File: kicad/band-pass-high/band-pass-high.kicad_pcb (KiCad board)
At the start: 2 copper layers, 154.9 x 25.4 mm, 66 parts, among them J1 Conn_01x06, U1 LF353DR, U2 LF353DR, U3 LF353DR, U4 LM339DR, U5 LM339DR

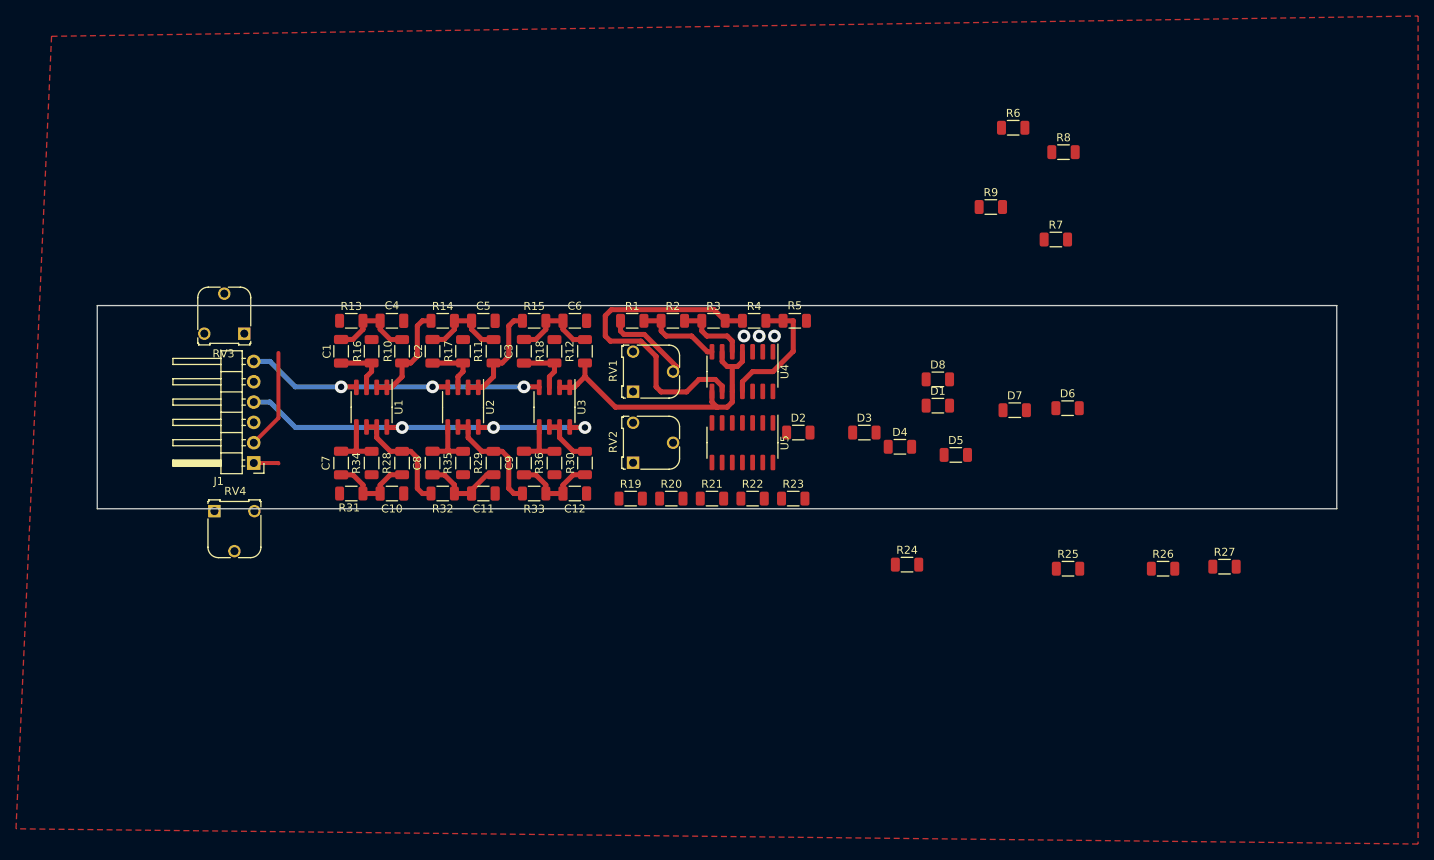
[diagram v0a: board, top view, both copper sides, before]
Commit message: Made a filter PCB design
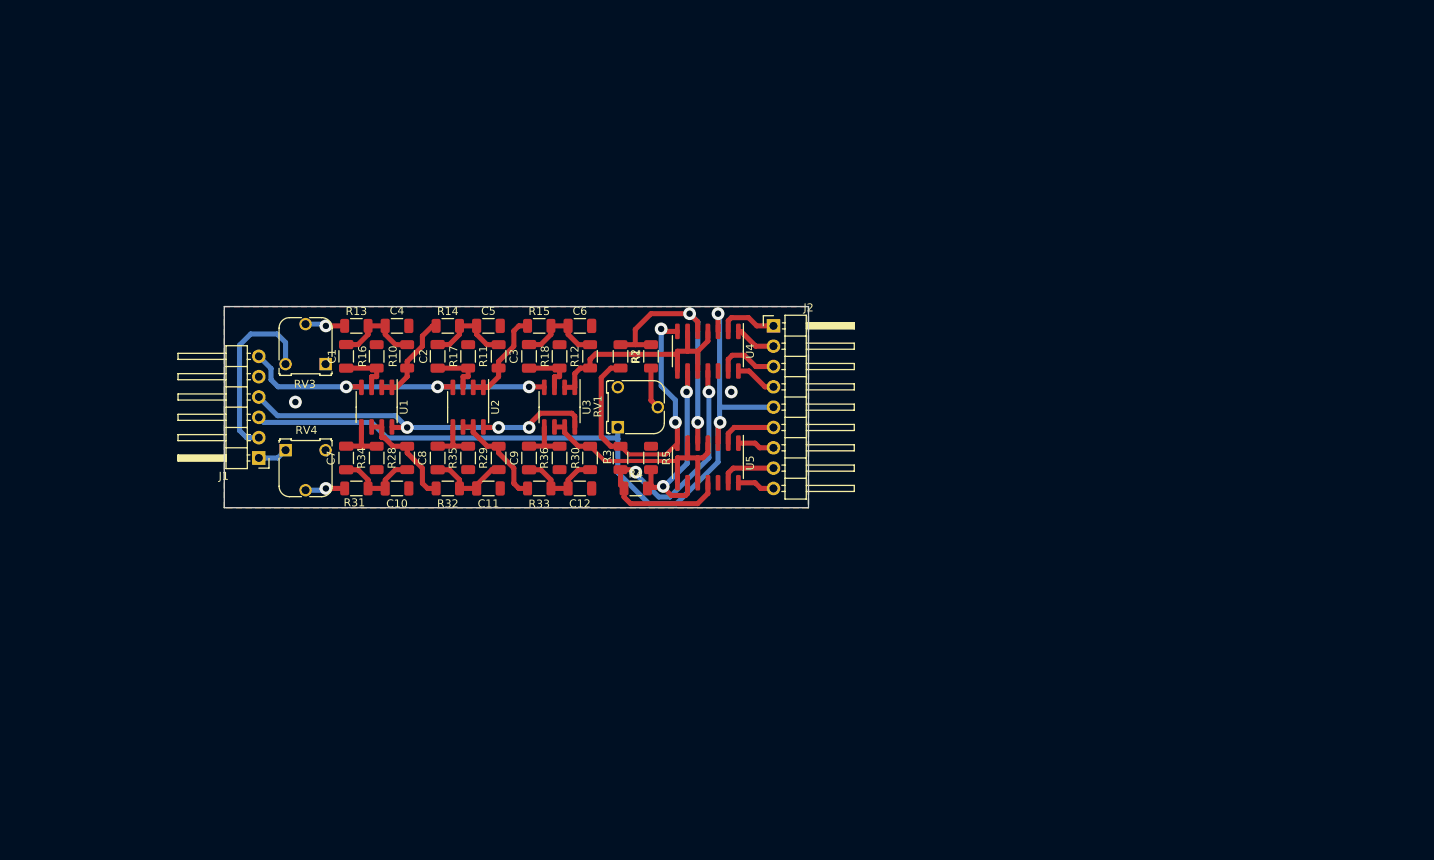
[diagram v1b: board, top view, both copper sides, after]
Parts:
- removed D1, D5: blue, Resistor_SMD:R_1206_3216Metric
- removed D2, D6: green, Resistor_SMD:R_1206_3216Metric
- removed D3, D7: yellow, Resistor_SMD:R_1206_3216Metric
- removed D4, D8: orange, Resistor_SMD:R_1206_3216Metric
- removed R19, R20, R21, R22, R23: 100k, Resistor_SMD:R_1206_3216Metric
- removed R24, R25, R26, R27, R7, R8, R9: R, Resistor_SMD:R_1206_3216Metric
- removed R6: BLUe, Resistor_SMD:R_1206_3216Metric
- removed RV2: 10k, Potentiometer_THT:Potentiometer_Runtron_RM-065_Vertical
- added J2: Conn_01x09_Male, Connector_PinHeader_2.54mm:PinHeader_1x09_P2.54mm_Horizontal, F.Cu at (185.5, 64.1)
- moved R4 25.7 mm to (168.3, 84.5)
- moved R5 24.8 mm to (170.2, 80.6), turned to 90 degrees
- moved R3 20.7 mm to (166.4, 80.6), turned to -90 degrees
- moved RV4 11.7 mm to (124.5, 79.7)
- moved RV3 10.9 mm to (129.5, 68.9)
- moved R2 7.91 mm to (166.4, 67.9), turned to -90 degrees
- moved R1 5.03 mm to (170.2, 67.9), turned to 90 degrees
- moved U4 5.01 mm to (177.3, 67.3)
- moved U5 5.00 mm to (177.3, 81.3)
- moved RV1 4.84 mm to (166.0, 76.8)
- moved C10 0.90 mm to (138.4, 84.5)
- moved C11 0.90 mm to (149.9, 84.5)
- moved C4 0.90 mm to (138.4, 64.1)
- moved C5 0.90 mm to (149.9, 64.1)
- moved C7 0.90 mm to (132.1, 80.6)
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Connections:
- U4 pad 11: Net-(R4-Pad2) -> Net-(R3-Pad2)
- U4 pad 5: Net-(R2-Pad2) -> Net-(R1-Pad2)
- U4 pad 7: Net-(R1-Pad2) -> Net-(R2-Pad2)
- U4 pad 9: Net-(R3-Pad2) -> Net-(R4-Pad2)
- U5 pad 11: Net-(U5-Pad11) -> Net-(R3-Pad2)
- U5 pad 5: Net-(U5-Pad5) -> Net-(R1-Pad2)
- U5 pad 7: Net-(R19-Pad2) -> Net-(R2-Pad2)
- U5 pad 9: Net-(R21-Pad2) -> Net-(R4-Pad2)
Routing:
- net +5V: track 0.00 -> 98.4 mm, vias 0 -> 2
- net Net-(R2-Pad2): track 9.10 -> 38.7 mm, vias 0 -> 2
- net Net-(R30-Pad2): track 6.49 -> 30.9 mm
- net Net-(R1-Pad2): track 10.9 -> 32.8 mm, vias 0 -> 2
- net Net-(J1-Pad2): track 12.5 -> 22.9 mm
- net Net-(R4-Pad2): track 16.4 -> 25.2 mm, vias 0 -> 2
- net Net-(U4-Pad13): track 0.00 -> 7.91 mm
- net Net-(U4-Pad2): track 0.00 -> 7.58 mm
- net Net-(R12-Pad2): track 37.9 -> 30.5 mm
- net Net-(U5-Pad2): track 0.00 -> 7.19 mm
- net Net-(U5-Pad13): track 0.00 -> 7.12 mm
- net Net-(R1-Pad1): track 10.9 -> 5.24 mm
- net Net-(U4-Pad14): track 0.00 -> 5.21 mm
- net Net-(U4-Pad1): track 0.00 -> 5.15 mm
- net audio_left: track 0.00 -> 4.98 mm, vias 0 -> 1
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- added copper zone on B.Cu, net GND
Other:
- board size 154.9 x 25.4 mm -> 73 x 25.1 mm

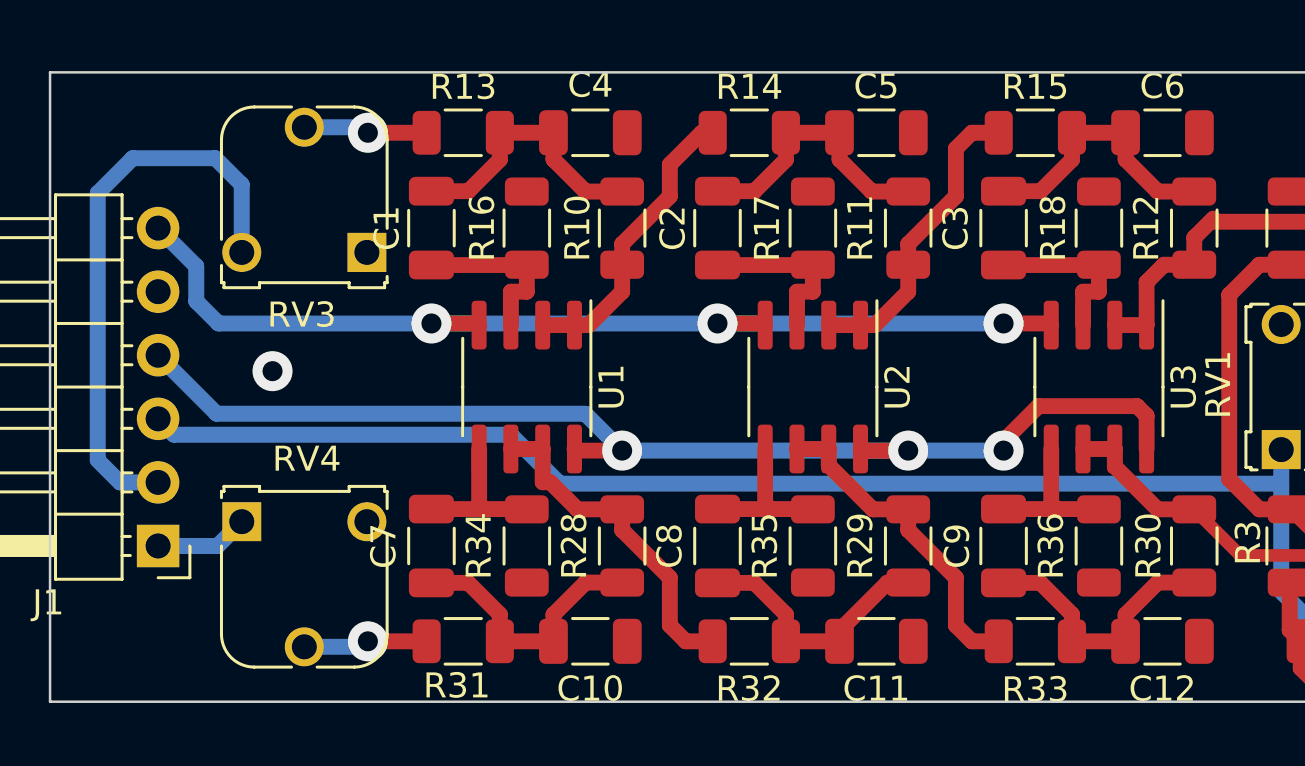
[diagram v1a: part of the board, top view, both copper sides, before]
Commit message: Found a better way with less vias
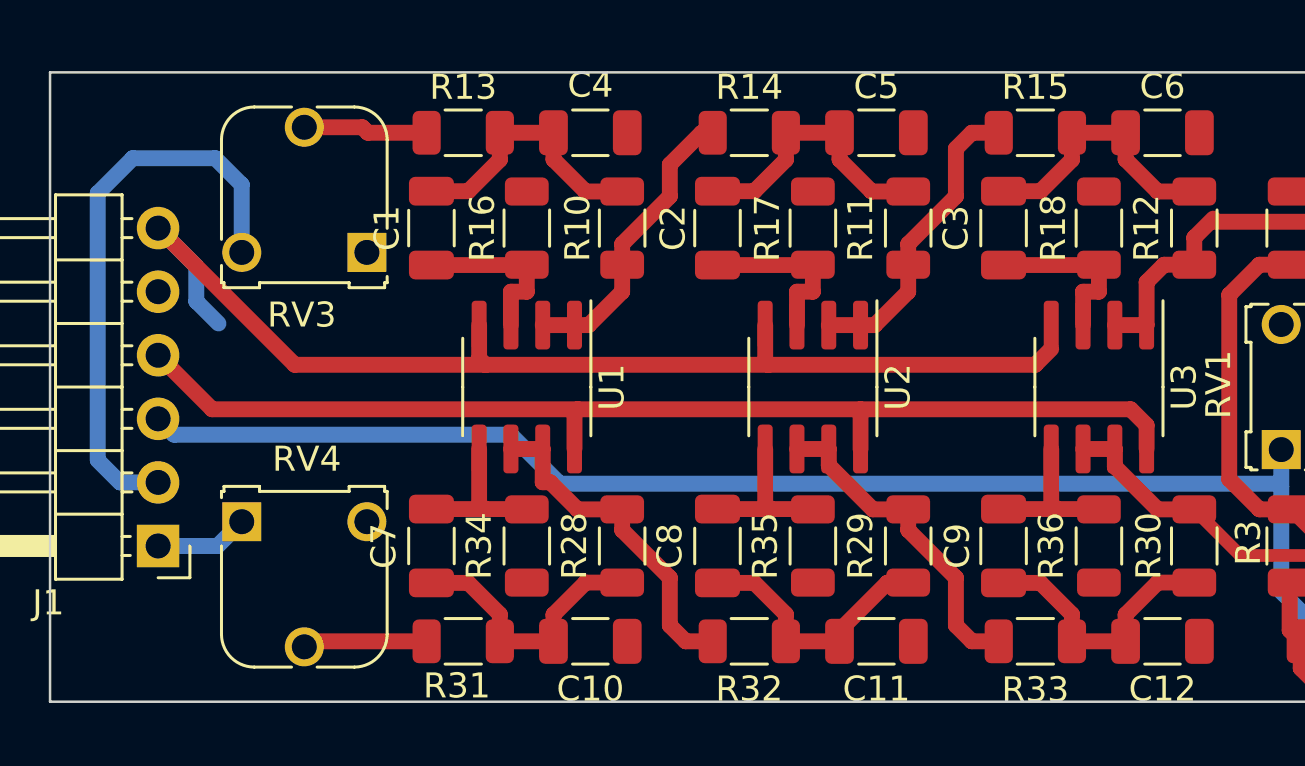
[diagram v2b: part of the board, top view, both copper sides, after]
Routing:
- net -15V: track 42.0 -> 46.4 mm, vias 3 -> 0
- net +15V: track 47.4 -> 44.8 mm, vias 3 -> 0
- net audio_right: vias 1 -> 0
- net audio_left: vias 1 -> 0
- net GND: vias 2 -> 1
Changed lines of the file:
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@@
   )
   (gr_rect (start 116.84 61.722) (end 189.865 86.868) (layer "Edge.Cuts") (width 0.1) (fill none))
-  (via (at 125.73 73.66) (size 1.6) (drill 0.8) (layers "F.Cu" "B.Cu") (free) (net 1))
   (via (at 180.213 72.39) (size 1.6) (drill 0.8) (layers "F.Cu" "B.Cu") (free) (net 1))
-  (segment (start 129.54 84.455) (end 131.8875 84.455) (width 0.635) (layer "F.Cu") (net 2))
-  (via (at 129.54 84.455) (size 1.6) (drill 0.8) (layers "F.Cu" "B.Cu") (net 2))
-  (segment (start 129.32 84.675) (end 129.54 84.455) (width 0.635) (layer "B.Cu") (net 2))
-  (segment (start 127 84.675) (end 129.32 84.675) (width 0.635) (layer "B.Cu") (net 2))
+  (segment (start 127.22 84.455) (end 127 84.675) (width 0.635) (layer "F.Cu") (net 2))
+  (segment (start 131.8875 84.455) (end 127.22 84.455) (width 0.635) (layer "F.Cu") (net 2))
+  (segment (start 129.32 63.915) (end 129.54 64.135) (width 0.635) (layer "F.Cu") (net 3))
   (segment (start 129.54 64.135) (end 131.8875 64.135) (width 0.635) (layer "F.Cu") (net 3))
-  (via (at 129.54 64.135) (size 1.6) (drill 0.8) (layers "F.Cu" "B.Cu") (net 3))
-  (segment (start 127 63.915) (end 129.32 63.915) (width 0.635) (layer "B.Cu") (net 3))
-  (segment (start 129.32 63.915) (end 129.54 64.135) (width 0.635) (layer "B.Cu") (net 3))
+  (segment (start 127 63.915) (end 129.32 63.915) (width 0.635) (layer "F.Cu") (net 3))
   (segment (start 178.562 78.795) (end 178.562 76.073) (width 0.635) (layer "F.Cu") (net 4))
   (segment (start 178.562 64.825) (end 178.562 62.611) (width 0.635) (layer "F.Cu") (net 4))
@@
   (segment (start 178.562 81.153) (end 178.562 76.073) (width 0.635) (layer "B.Cu") (net 4))
   (segment (start 178.562 62.611) (end 178.7525 62.8015) (width 0.635) (layer "B.Cu") (net 4))
-  (segment (start 143.51 71.755) (end 145.35 71.755) (width 0.635) (layer "F.Cu") (net 5))
-  (segment (start 154.94 71.755) (end 156.78 71.755) (width 0.635) (layer "F.Cu") (net 5))
-  (segment (start 156.78 71.755) (end 156.845 71.82) (width 0.635) (layer "F.Cu") (net 5))
-  (segment (start 132.08 71.755) (end 133.92 71.755) (width 0.635) (layer "F.Cu") (net 5))
-  (segment (start 133.92 71.755) (end 133.985 71.82) (width 0.635) (layer "F.Cu") (net 5))
-  (segment (start 145.35 71.755) (end 145.415 71.82) (width 0.635) (layer "F.Cu") (net 5))
-  (via (at 143.51 71.755) (size 1.6) (drill 0.8) (layers "F.Cu" "B.Cu") (net 5))
-  (via (at 154.94 71.755) (size 1.6) (drill 0.8) (layers "F.Cu" "B.Cu") (net 5))
-  (via (at 132.08 71.755) (size 1.6) (drill 0.8) (layers "F.Cu" "B.Cu") (net 5))
-  (segment (start 143.51 71.755) (end 154.94 71.755) (width 0.635) (layer "B.Cu") (net 5))
-  (segment (start 123.571 71.755) (end 132.08 71.755) (width 0.635) (layer "B.Cu") (net 5))
+  (segment (start 145.542 73.406) (end 156.21 73.406) (width 0.635) (layer "F.Cu") (net 5))
+  (segment (start 134.239 73.406) (end 126.619 73.406) (width 0.635) (layer "F.Cu") (net 5))
+  (segment (start 145.415 71.82) (end 145.415 73.279) (width 0.635) (layer "F.Cu") (net 5))
+  (segment (start 133.985 71.82) (end 133.985 73.152) (width 0.635) (layer "F.Cu") (net 5))
+  (segment (start 133.985 73.152) (end 134.239 73.406) (width 0.635) (layer "F.Cu") (net 5))
+  (segment (start 134.239 73.406) (end 145.542 73.406) (width 0.635) (layer "F.Cu") (net 5))
+  (segment (start 156.21 73.406) (end 156.845 72.771) (width 0.635) (layer "F.Cu") (net 5))
+  (segment (start 145.415 73.279) (end 145.542 73.406) (width 0.635) (layer "F.Cu") (net 5))
+  (segment (start 126.619 73.406) (end 121.158 67.945) (width 0.635) (layer "F.Cu") (net 5))
   (segment (start 121.158 67.945) (end 122.682 69.469) (width 0.635) (layer "B.Cu") (net 5))
   (segment (start 122.682 69.469) (end 122.682 70.866) (width 0.635) (layer "B.Cu") (net 5))
   (segment (start 122.682 70.866) (end 123.571 71.755) (width 0.635) (layer "B.Cu") (net 5))
-  (segment (start 132.08 71.755) (end 143.51 71.755) (width 0.635) (layer "B.Cu") (net 5))
-  (segment (start 160.274 75.057) (end 156.337 75.057) (width 0.635) (layer "F.Cu") (net 6))
-  (segment (start 154.94 76.454) (end 154.94 76.835) (width 0.635) (layer "F.Cu") (net 6))
-  (segment (start 151.13 76.835) (end 149.29 76.835) (width 0.635) (layer "F.Cu") (net 6))
-  (segment (start 149.29 76.835) (end 149.225 76.77) (width 0.635) (layer "F.Cu") (net 6))
-  (segment (start 160.655 76.77) (end 160.655 75.438) (width 0.635) (layer "F.Cu") (net 6))
-  (segment (start 139.7 76.835) (end 137.86 76.835) (width 0.635) (layer "F.Cu") (net 6))
-  (segment (start 137.86 76.835) (end 137.795 76.77) (width 0.635) (layer "F.Cu") (net 6))
-  (segment (start 160.655 75.438) (end 160.274 75.057) (width 0.635) (layer "F.Cu") (net 6))
-  (segment (start 156.337 75.057) (end 154.94 76.454) (width 0.635) (layer "F.Cu") (net 6))
-  (via (at 139.7 76.835) (size 1.6) (drill 0.8) (layers "F.Cu" "B.Cu") (net 6))
-  (via (at 151.13 76.835) (size 1.6) (drill 0.8) (layers "F.Cu" "B.Cu") (net 6))
-  (via (at 154.94 76.835) (size 1.6) (drill 0.8) (layers "F.Cu" "B.Cu") (net 6))
-  (segment (start 139.7 76.835) (end 151.13 76.835) (width 0.635) (layer "B.Cu") (net 6))
-  (segment (start 121.158 73.025) (end 123.495281 75.362281) (width 0.635) (layer "B.Cu") (net 6))
-  (segment (start 151.13 76.835) (end 154.94 76.835) (width 0.635) (layer "B.Cu") (net 6))
-  (segment (start 138.22728 75.36228) (end 139.7 76.835) (width 0.635) (layer "B.Cu") (net 6))
-  (segment (start 123.495281 75.362281) (end 138.22728 75.36228) (width 0.635) (layer "B.Cu") (net 6))
+  (segment (start 149.225 76.77) (end 149.225 75.184) (width 0.635) (layer "F.Cu") (net 6))
+  (segment (start 137.922 75.184) (end 123.317 75.184) (width 0.635) (layer "F.Cu") (net 6))
+  (segment (start 160.655 76.77) (end 160.655 75.819) (width 0.635) (layer "F.Cu") (net 6))
+  (segment (start 137.922 75.184) (end 149.225 75.184) (width 0.635) (layer "F.Cu") (net 6))
+  (segment (start 137.795 76.77) (end 137.795 75.311) (width 0.635) (layer "F.Cu") (net 6))
+  (segment (start 149.225 75.184) (end 160.02 75.184) (width 0.635) (layer "F.Cu") (net 6))
+  (segment (start 160.655 75.819) (end 160.02 75.184) (width 0.635) (layer "F.Cu") (net 6))
+  (segment (start 123.317 75.184) (end 121.158 73.025) (width 0.635) (layer "F.Cu") (net 6))
+  (segment (start 137.795 75.311) (end 137.922 75.184) (width 0.635) (layer "F.Cu") (net 6))
   (segment (start 138.2375 66.4825) (end 139.7 66.4825) (width 0.635) (layer "F.Cu") (net 7))
   (segment (start 136.955 64.135) (end 136.955 65.2) (width 0.635) (layer "F.Cu") (net 7))
